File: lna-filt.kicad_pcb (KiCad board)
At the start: 2 copper layers, 51 x 56 mm, 27 parts, among them J1 Conn_Coaxial, J2 Conn_Coaxial, J3 Barrel_Jack, J4 USB_B_Micro, J5 Conn_Coaxial, J6 Conn_Coaxial, U1 HMC374, U2 MCP1703A-3302_SOT223

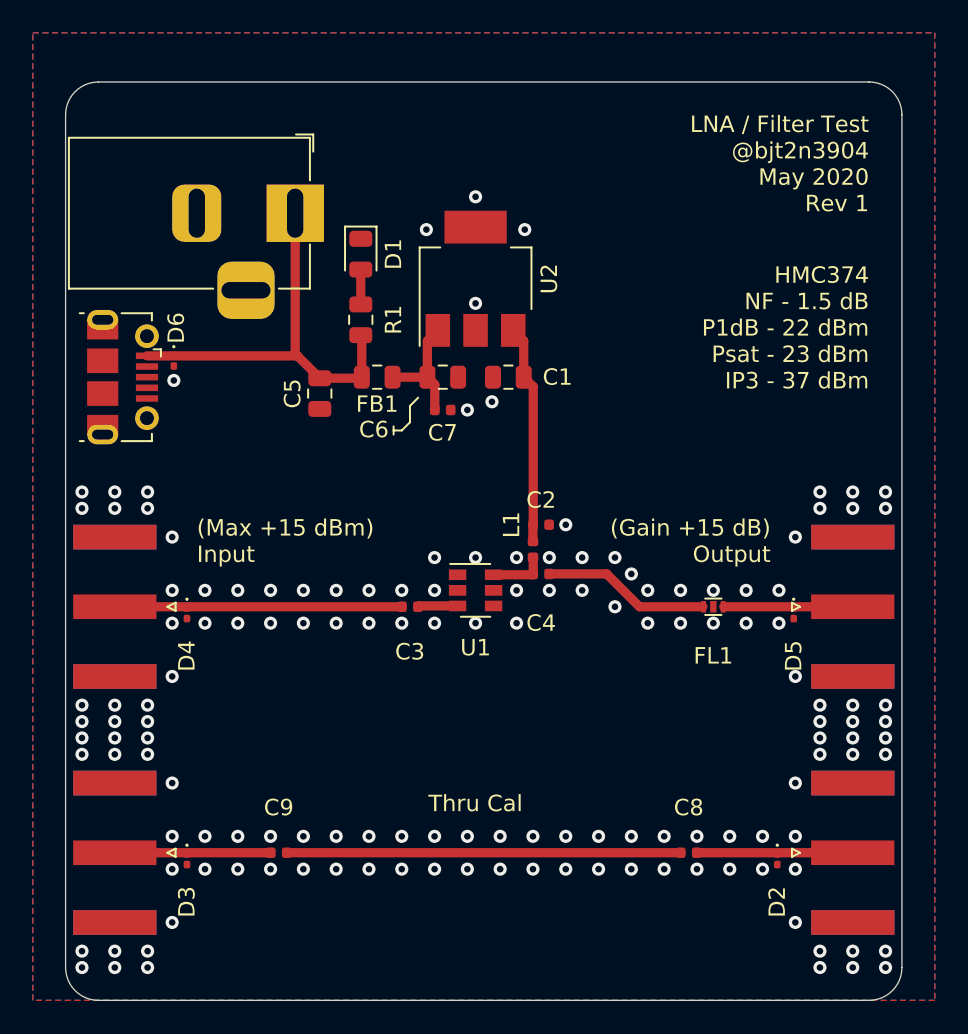
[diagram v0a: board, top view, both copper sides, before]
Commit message: Move LED to 3V3, add power silk screen
Closes #2
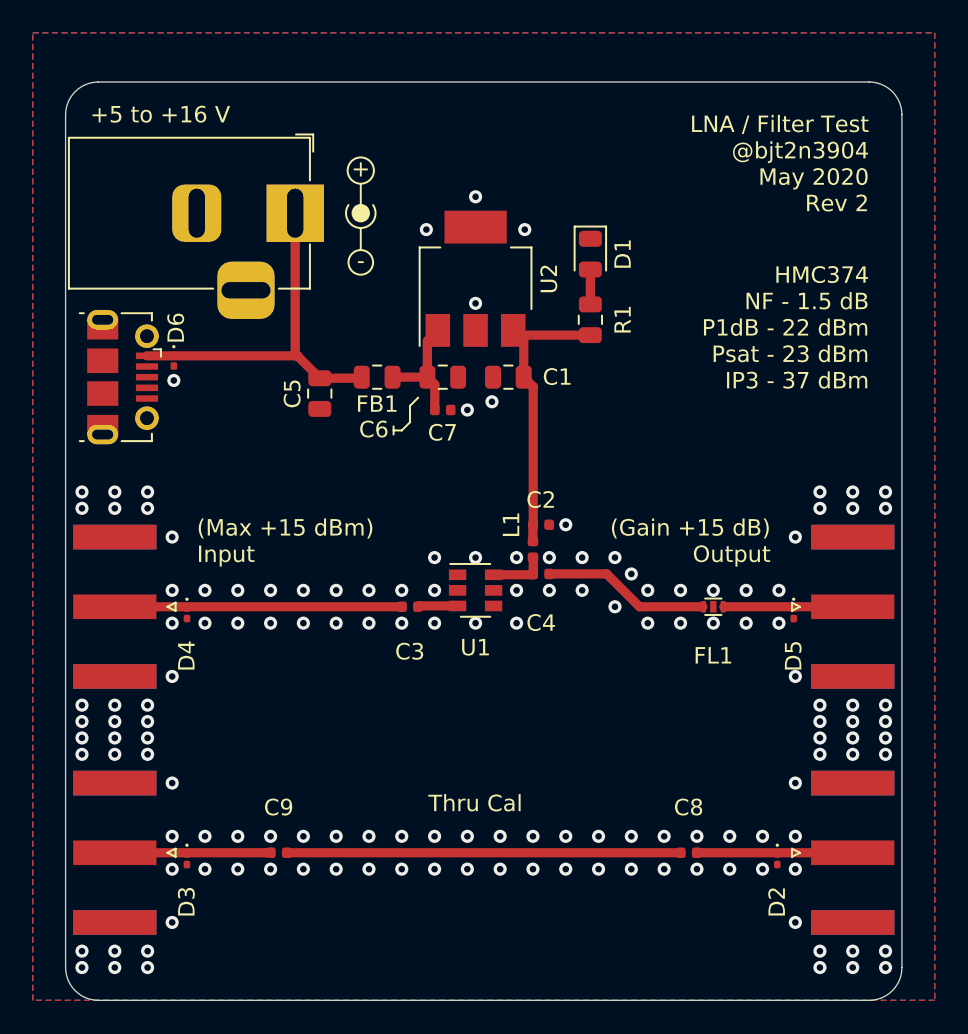
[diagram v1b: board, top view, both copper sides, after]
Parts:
- moved D1 14.0 mm to (114.0, 38.5)
- moved R1 14.0 mm to (114.0, 42.5)
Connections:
- R1 pad 2: +5V -> +3V3
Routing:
- net +3V3: track 13.4 -> 18.3 mm
- net +5V: track 25.0 -> 22.4 mm
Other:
- board text added: "+"
- board text added: "+5 to +16 V"
- board text added: "-"
- board text added: "LNA / Filter Test @bjt2n3904 May 2020 Rev 2"
- board text removed: "LNA / Filter Test @bjt2n3904 May 2020 Rev 1"
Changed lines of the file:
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@@
   (general
     (thickness 1.6)
-    (drawings 20)
-    (tracks 180)
+    (drawings 35)
+    (tracks 181)
     (zones 0)
     (modules 27)
@@
   )
   (module Resistor_SMD:R_0805_2012Metric (layer F.Cu)
-    (at 100 42.5 270)
+    (at 114 42.5 270)
     (descr "Resistor SMD 0805 (2012 Metric), square (rectangular) end terminal, IPC_7351 nominal, (Body size source: https://docs.google.com/spreadsheets/d/1BsfQQcO9C6DZCsRaXUlFlo91Tg2WpOkGARC1WS5S8t0/edit?usp=sharing), generated with kicad-footprint-generator")
     (tags resistor)
@@
     (fp_line (start -1 0.6) (end -1 -0.6) (layer F.Fab) (width 0.1))
     (pad 2 smd roundrect (at 0.9375 0 270) (size 0.975 1.4) (layers F.Cu F.Paste F.Mask) (roundrect_rratio 0.25)
-      (net 7 +5V))
+      (net 1 +3V3))
     (pad 1 smd roundrect (at -0.9375 0 270) (size 0.975 1.4) (layers F.Cu F.Paste F.Mask) (roundrect_rratio 0.25)
       (net 9 "Net-(D1-Pad2)"))
@@
   )
   (module LED_SMD:LED_0805_2012Metric (layer F.Cu)
-    (at 100 38.5 270)
+    (at 114 38.5 270)
     (descr "LED SMD 0805 (2012 Metric), square (rectangular) end terminal, IPC_7351 nominal, (Body size source: https://docs.google.com/spreadsheets/d/1BsfQQcO9C6DZCsRaXUlFlo91Tg2WpOkGARC1WS5S8t0/edit?usp=sharing), generated with kicad-footprint-generator")
     (tags diode)
@@
     )
   )
+  (gr_circle (center 100 33.4) (end 100 34.2) (layer F.SilkS) (width 0.12))
+  (gr_circle (center 100 39) (end 100 38.25) (layer F.SilkS) (width 0.12))
+  (gr_line (start 100 36) (end 100 35.9) (layer F.SilkS) (width 0.12))
+  (gr_circle (center 100 36) (end 100 35.8) (layer F.SilkS) (width 0.12))
+  (gr_circle (center 100 36) (end 100.1 35.7) (layer F.SilkS) (width 0.12))
+  (gr_circle (center 100 36) (end 100 35.9) (layer F.SilkS) (width 0.12))
+  (gr_circle (center 100 36) (end 100 35.6) (layer F.SilkS) (width 0.12))
+  (gr_circle (center 100 36) (end 100 35.75) (layer F.SilkS) (width 0.12))
+  (gr_text - (at 100 38.9) (layer F.SilkS)
+    (effects (font (size 1 1) (thickness 0.15)))
+  )
+  (gr_line (start 100 36.9) (end 100 38.25) (layer F.SilkS) (width 0.12))
+  (gr_text + (at 100 33.3) (layer F.SilkS)
+    (effects (font (size 1 1) (thickness 0.15)))
+  )
+  (gr_line (start 100 35.5) (end 100 34.25) (layer F.SilkS) (width 0.12))
+  (gr_arc (start 100 36) (end 99.250001 35.500001) (angle -247.3801351) (layer F.SilkS) (width 0.12))
+  (gr_circle (center 100 36) (end 100 35.5) (layer F.SilkS) (width 0.12))
+  (gr_text "+5 to +16 V" (at 83.5 30) (layer F.SilkS)
+    (effects (font (size 1 1) (thickness 0.15)) (justify left))
+  )
   (gr_text "HMC374\nNF - 1.5 dB\nP1dB - 22 dBm\nPsat - 23 dBm\nIP3 - 37 dBm" (at 131 43) (layer F.SilkS)
     (effects (font (size 1 1) (thickness 0.15)) (justify right))
@@
     (effects (font (size 1 1) (thickness 0.15)) (justify left))
   )
-  (gr_text "LNA / Filter Test\n@bjt2n3904\nMay 2020\nRev 1" (at 131 33) (layer F.SilkS)
+  (gr_text "LNA / Filter Test\n@bjt2n3904\nMay 2020\nRev 2" (at 131 33) (layer F.SilkS)
     (effects (font (size 1 1) (thickness 0.15)) (justify right))
   )
@@
   (segment (start 96 44.5625) (end 96 36) (width 0.56388) (layer F.Cu) (net 7))
   (segment (start 96.1375 44.7) (end 96 44.5625) (width 0.56388) (layer F.Cu) (net 7))
-  (segment (start 100.0625 43.5) (end 100 43.4375) (width 0.56388) (layer F.Cu) (net 7))
-  (segment (start 100.0625 46) (end 100.0625 43.5) (width 0.56388) (layer F.Cu) (net 7))
+  (segment (start 114.0625 43.5) (end 114 43.4375) (width 0.56388) (layer F.Cu) (net 1))
+  (segment (start 109.5875 43.4375) (end 109.3 43.15) (width 0.56388) (layer F.Cu) (net 1))
+  (segment (start 114 43.4375) (end 109.5875 43.4375) (width 0.56388) (layer F.Cu) (net 1))
   (segment (start 101.9375 46) (end 104.0625 46) (width 0.56388) (layer F.Cu) (net 8))
   (segment (start 104.515 46.4525) (end 104.0625 46) (width 0.56388) (layer F.Cu) (net 8))
@@
   (segment (start 104.0625 43.7875) (end 104.7 43.15) (width 0.56388) (layer F.Cu) (net 8))
   (segment (start 104.0625 46) (end 104.0625 43.7875) (width 0.56388) (layer F.Cu) (net 8))
-  (segment (start 100 41.5625) (end 100 39.4375) (width 0.56388) (layer F.Cu) (net 9))
-  (segment (start 130 60) (end 122.134341 60) (width 0.56388) (layer F.Cu) (net 19))
+  (segment (start 114 41.5625) (end 114 39.4375) (width 0.56388) (layer F.Cu) (net 9))
   (segment (start 120.485 75) (end 130 75) (width 0.56388) (layer F.Cu) (net 16))
   (segment (start 95.485 75) (end 119.515 75) (width 0.56388) (layer F.Cu) (net 17))
   (segment (start 94.22 75) (end 85 75) (width 0.56388) (layer F.Cu) (net 18))
   (segment (start 94.515 75) (end 94.22 75) (width 0.56388) (layer F.Cu) (net 18))
+  (segment (start 130 60) (end 122.134341 60) (width 0.56388) (layer F.Cu) (net 19))
   (zone (net 2) (net_name GND) (layer F.Cu) (hatch edge 0.508)
     (connect_pads (clearance 0.1524))

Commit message: Removing thermals for SMA, fixing SMA short
The SMA connectors were not close enough to the edge of the PCB. A thin
strip of copper went under the center pin, and would short it to ground.
By bumping the connector closer to the PCB edge, we remove the short.

Closes #1.
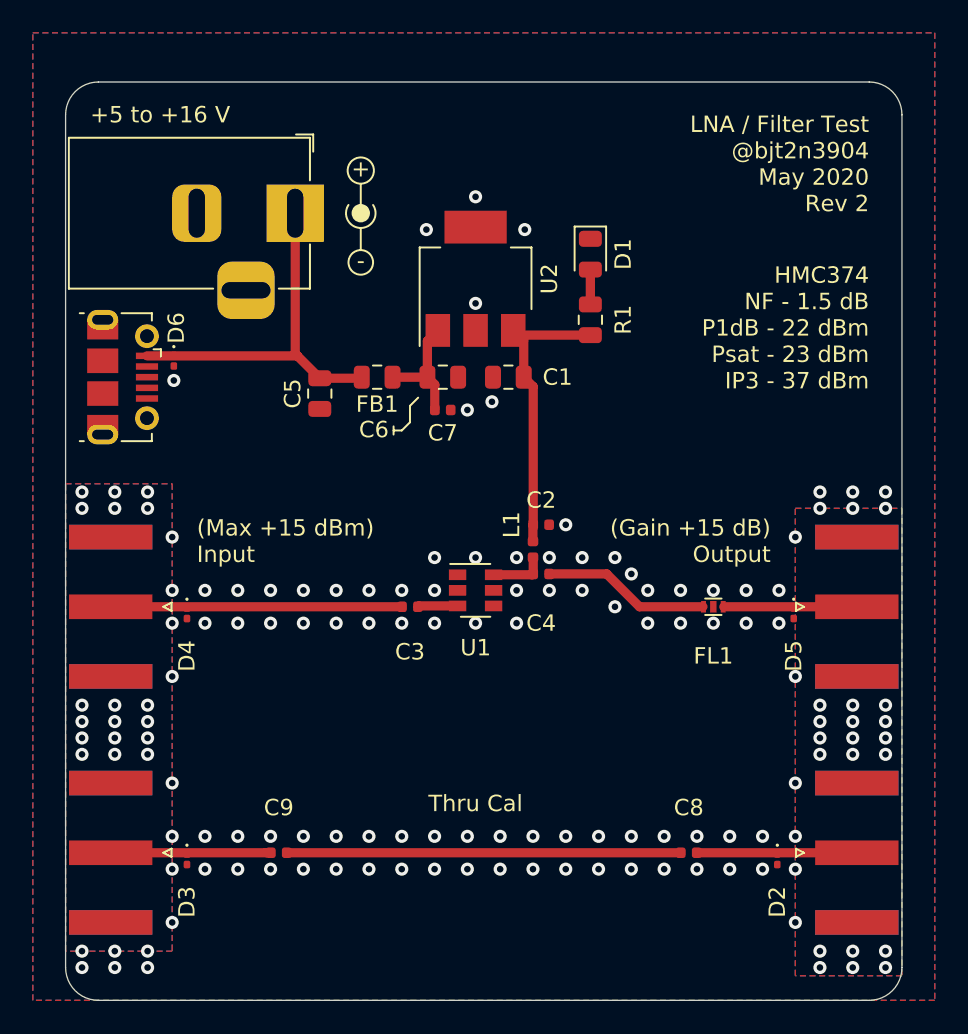
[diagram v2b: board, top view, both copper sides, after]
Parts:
- moved J1 0.25 mm to (84.8, 60.0)
- moved J2 0.25 mm to (130.2, 60.0)
- moved J5 0.25 mm to (130.2, 75.0)
- moved J6 0.25 mm to (84.8, 75.0)
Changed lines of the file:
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@@
   )
   (module Connector_Coaxial:SMA_Amphenol_132289_EdgeMount (layer F.Cu)
-    (at 85 75 180)
+    (at 84.75 75 180)
     (descr http://www.amphenolrf.com/132289.html)
     (tags SMA)
@@
   )
   (module Connector_Coaxial:SMA_Amphenol_132289_EdgeMount (layer F.Cu)
-    (at 130 75)
+    (at 130.25 75)
     (descr http://www.amphenolrf.com/132289.html)
     (tags SMA)
@@
   )
   (module Connector_Coaxial:SMA_Amphenol_132289_EdgeMount (layer F.Cu)
-    (at 130 60)
+    (at 130.25 60)
     (descr http://www.amphenolrf.com/132289.html)
     (tags SMA)
@@
   )
   (module Connector_Coaxial:SMA_Amphenol_132289_EdgeMount (layer F.Cu)
-    (at 85 60 180)
+    (at 84.75 60 180)
     (descr http://www.amphenolrf.com/132289.html)
     (tags SMA)
@@
     (polygon
       (pts
-        (xy 118 58) (xy 133 58) (xy 133 62) (xy 116 62) (xy 114 60)
-        (xy 108.5 60) (xy 108.5 56) (xy 116 56)
+        (xy 117.75 58.25) (xy 126.75 58.25) (xy 126.75 54.75) (xy 132.75 54.75) (xy 132.75 65.75)
+        (xy 126.75 65.75) (xy 126.75 62.25) (xy 115.75 62.25) (xy 113.75 60.25) (xy 110.7 60.25)
+        (xy 108.8 58.35) (xy 108.65 58.35) (xy 108.65 57.75) (xy 108.75 57.75) (xy 110.25 56.25)
+        (xy 115.75 56.25)
       )
     )
@@
     (polygon
       (pts
-        (xy 105.5 62) (xy 82 62) (xy 82 58) (xy 105.5 58)
+        (xy 105.25 59.65) (xy 105.4 59.65) (xy 105.4 60.25) (xy 105.25 60.25) (xy 103.5 62)
+        (xy 88 62) (xy 88 65.5) (xy 82 65.5) (xy 82 54.5) (xy 88 54.5)
+        (xy 88 58) (xy 103.6 58)
       )
     )
@@
     (polygon
       (pts
-        (xy 133 73) (xy 133 77) (xy 82 77) (xy 82 73)
-      )
-    )
+        (xy 88 69.5) (xy 88 73) (xy 127 73) (xy 127 69.5) (xy 133 69.5)
+        (xy 133 80.5) (xy 127 80.5) (xy 127 77) (xy 88 77) (xy 88 80.5)
+        (xy 82 80.5) (xy 82 69.5)
+      )
+    )
+  )
+  (zone (net 2) (net_name GND) (layer F.Cu) (hatch edge 0.508)
+    (connect_pads (clearance 0.1524))
+    (min_thickness 0.254)
+    (fill yes (arc_segments 32) (thermal_gap 0) (thermal_bridge_width 0.508))
+    (polygon
+      (pts
+        (xy 88.5 81) (xy 82 81) (xy 82 52.5) (xy 88.5 52.5)
+      )
+    )
+  )
+  (zone (net 2) (net_name GND) (layer F.Cu) (hatch edge 0.508)
+    (connect_pads (clearance 0.1524))
+    (min_thickness 0.254)
+    (fill yes (arc_segments 32) (thermal_gap 0) (thermal_bridge_width 0.508))
+    (polygon
+      (pts
+        (xy 126.5 54) (xy 133 54) (xy 133 82.5) (xy 126.5 82.5)
+      )
+    )
+  )
+  (zone (net 2) (net_name GND) (layer B.Cu) (hatch edge 0.508)
+    (connect_pads (clearance 0.1524))
+    (min_thickness 0.254)
+    (fill yes (arc_segments 32) (thermal_gap 0) (thermal_bridge_width 0.508))
+    (polygon
+      (pts
+        (xy 88.5 81) (xy 82 81) (xy 82 52.5) (xy 88.5 52.5)
+      )
+    )
+  )
+  (zone (net 2) (net_name GND) (layer B.Cu) (hatch edge 0.508)
+    (connect_pads (clearance 0.1524))
+    (min_thickness 0.254)
+    (fill yes (arc_segments 32) (thermal_gap 0) (thermal_bridge_width 0.508))
+    (polygon
+      (pts
+        (xy 126.5 54) (xy 133 54) (xy 133 82.5) (xy 126.5 82.5)
+      )
+    )
+  )
+  (zone (net 0) (net_name "") (layer B.Mask) (hatch edge 0.508)
+    (connect_pads (clearance 0.1524))
+    (min_thickness 0.254)
+    (fill yes (arc_segments 32) (thermal_gap 0) (thermal_bridge_width 0.508))
+    (polygon
+      (pts
+        (xy 88 58.5) (xy 82 58.5) (xy 82 54.5) (xy 88 54.5)
+      )
+    )
+  )
+  (zone (net 0) (net_name "") (layer B.Mask) (hatch edge 0.508)
+    (connect_pads (clearance 0.1524))
+    (min_thickness 0.254)
+    (fill yes (arc_segments 32) (thermal_gap 0) (thermal_bridge_width 0.508))
+    (polygon
+      (pts
+        (xy 88 65.5) (xy 82 65.5) (xy 82 61.5) (xy 88 61.5)
+      )
+    )
+  )
+  (zone (net 0) (net_name "") (layer B.Mask) (hatch edge 0.508)
+    (connect_pads (clearance 0.1524))
+    (min_thickness 0.254)
+    (fill yes (arc_segments 32) (thermal_gap 0) (thermal_bridge_width 0.508))
+    (polygon
+      (pts
+        (xy 88 73.5) (xy 82 73.5) (xy 82 69.5) (xy 88 69.5)
+      )
+    )
+  )
+  (zone (net 0) (net_name "") (layer B.Mask) (hatch edge 0.508)
+    (connect_pads (clearance 0.1524))
+    (min_thickness 0.254)
+    (fill yes (arc_segments 32) (thermal_gap 0) (thermal_bridge_width 0.508))
+    (polygon
+      (pts
+        (xy 88 80.5) (xy 82 80.5) (xy 82 76.5) (xy 88 76.5)
+      )
+    )
+  )
+  (zone (net 0) (net_name "") (layer B.Mask) (hatch edge 0.508)
+    (connect_pads (clearance 0.1524))
+    (min_thickness 0.254)
+    (fill yes (arc_segments 32) (thermal_gap 0) (thermal_bridge_width 0.508))
+    (polygon
+      (pts
+        (xy 133 80.5) (xy 127 80.5) (xy 127 76.5) (xy 133 76.5)
+      )
+    )
+  )
+  (zone (net 0) (net_name "") (layer B.Mask) (hatch edge 0.508)
+    (connect_pads (clearance 0.1524))
+    (min_thickness 0.254)
+    (fill yes (arc_segments 32) (thermal_gap 0) (thermal_bridge_width 0.508))
+    (polygon
+      (pts
+        (xy 133 73.5) (xy 127 73.5) (xy 127 69.5) (xy 133 69.5)
+      )
+    )
+  )
+  (zone (net 0) (net_name "") (layer B.Mask) (hatch edge 0.508)
+    (connect_pads (clearance 0.1524))
+    (min_thickness 0.254)
+    (fill yes (arc_segments 32) (thermal_gap 0) (thermal_bridge_width 0.508))
+    (polygon
+      (pts
+        (xy 133 58.5) (xy 127 58.5) (xy 127 54.5) (xy 133 54.5)
+      )
+    )
+  )
+  (zone (net 0) (net_name "") (layer B.Mask) (hatch edge 0.508)
+    (connect_pads (clearance 0.1524))
+    (min_thickness 0.254)
+    (fill yes (arc_segments 32) (thermal_gap 0) (thermal_bridge_width 0.508))
+    (polygon
+      (pts
+        (xy 133 65.5) (xy 127 65.5) (xy 127 61.5) (xy 133 61.5)
+      )
+    )
